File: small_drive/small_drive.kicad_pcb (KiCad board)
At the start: 2 copper layers, 100 x 80 mm, 159 parts, among them J1 DB9, J2 DB15, M1 SiR826DP, M2 SiR826DP, M3 SiR826DP, M4 SiR826DP, M5 SiR826DP, M6 SiR826DP, P1 CONN_01X04, P2 CONN_01X04, P3 CONN_01X04, P4 CONN_01X04, P5 CONN_01X02, P6 CONN_01X02, P7 CONN_01X02, P8 CONN_01X01, U1 XMC4400-F64x512, U10 LM5106, U11 ACS711KLCTR-12AB-T, U12 ACS711ELCTR-25AB-T, U13 ACS711KLCTR-12AB-T, U14 AD8226, U15 MAX3096, U16 AMC1203, U17 7805, U18 LT1764EQ, U19 KSZ8081, U2 ips511g, U20 ETH100_MAG, U3 ips511g, U4 LTC2850, U5 AD8226, U6 LT1764EQ, U7 MC33074DTBR2, U8 LM5106, U9 LM5106, X1 NKE1212DC, X2 NKE1212DC, X3 HCPL0201, X4 HCPL0201, X5 HCPL0201, X6 HCPL0201, Y1 12MHz, Y2 25MHz

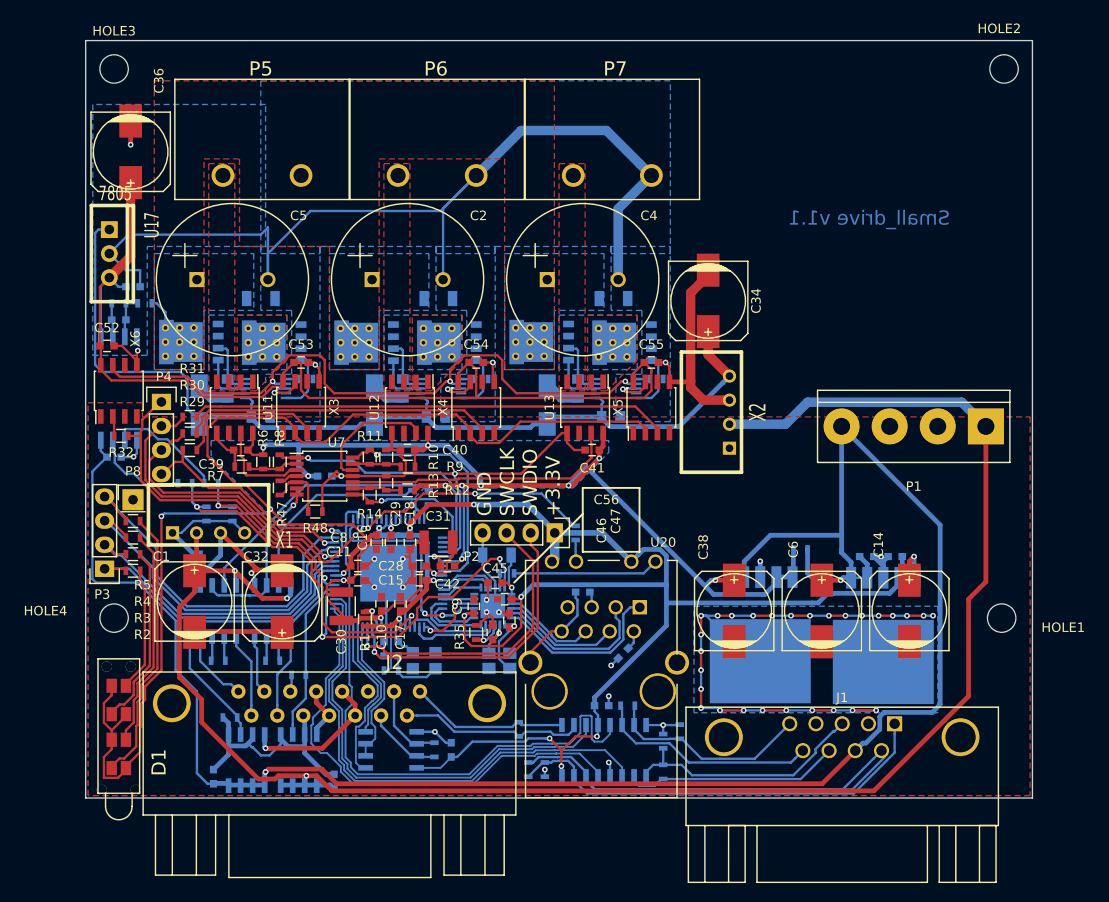
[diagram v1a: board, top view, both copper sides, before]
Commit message: Fully routed PCB with 100-pin package
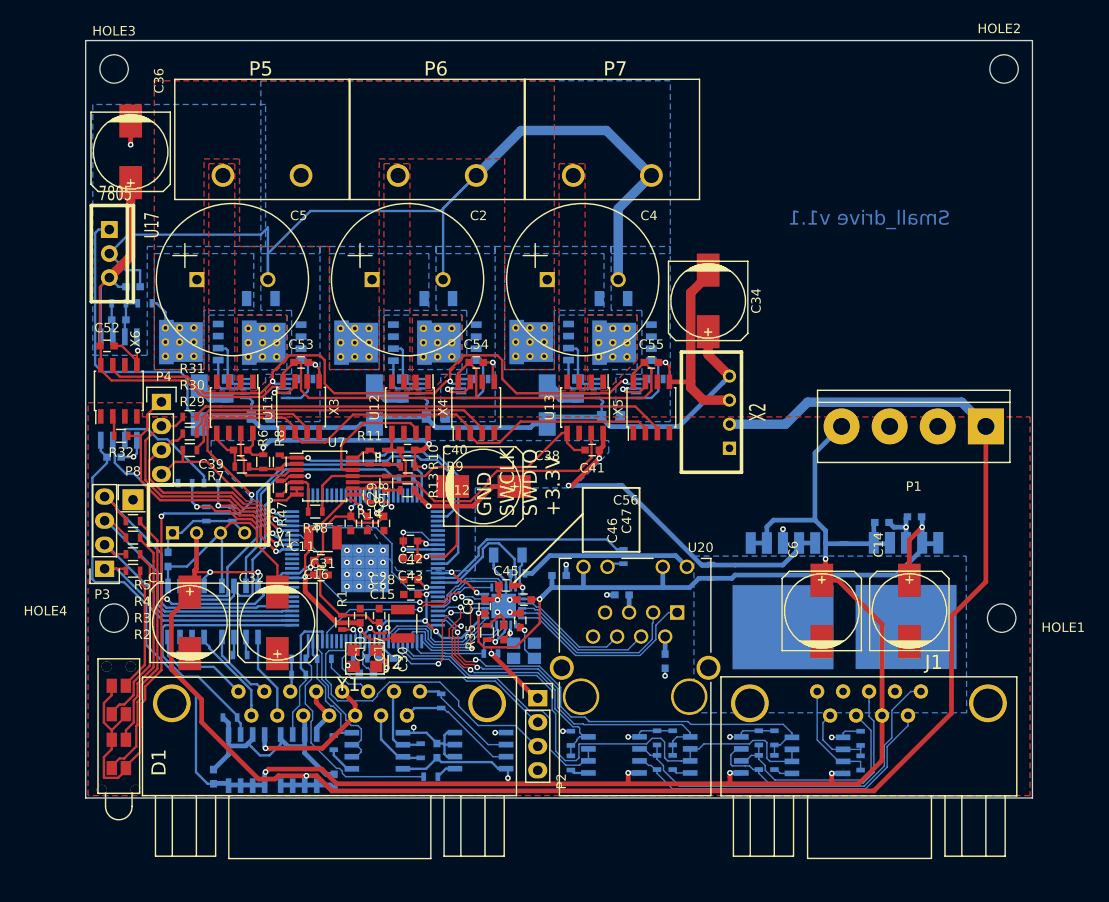
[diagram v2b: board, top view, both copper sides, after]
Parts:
- added R49: 1k, Resistors_SMD:R_0603, B.Cu at (81.8, 168.8)
- added R50: 510, Resistors_SMD:R_0603, B.Cu at (111.8, 180.2)
- added R51: 510, Resistors_SMD:R_0603, B.Cu at (101.0, 180.2)
- added R52: 510, Resistors_SMD:R_0603, B.Cu at (90.2, 180.3)
- added R53: 1k, Resistors_SMD:R_0603, B.Cu at (61.5, 169.3)
- added R54: 1k, Resistors_SMD:R_0603, B.Cu at (101.0, 177.7)
- added R55: 1k, Resistors_SMD:R_0603, B.Cu at (90.2, 177.7)
- added R56: 510, Resistors_SMD:R_0603, B.Cu at (75.5, 181.8)
- added R57: 510, Resistors_SMD:R_0603, B.Cu at (65.2, 178.2)
- added R58: 1k, Resistors_SMD:R_0603, B.Cu at (64.2, 169.3)
- added R59: 1k, Resistors_SMD:R_0603, B.Cu at (111.8, 177.7)
- added U21: MAX3463, Housings_SOIC:SOIC-8_3.9x4.9mm_Pitch1.27mm, B.Cu at (116.3, 179.5)
- added U22: MAX3463, Housings_SOIC:SOIC-8_3.9x4.9mm_Pitch1.27mm, B.Cu at (105.5, 179.4)
- added U23: MAX3463, Housings_SOIC:SOIC-8_3.9x4.9mm_Pitch1.27mm, B.Cu at (94.8, 179.4)
- C43, Y1: moved to F.Cu
- J1: footprint Connectors_Amphenol:DB9FC_HD-20 -> 00_Passives:DB9F_ebay
- J2: footprint Connectors_Amphenol:DB15F_HD20_SIZE2 -> 00_Passives:DB15F_ebay
- R22, R23: value R -> 4.7k
- R25, R26: value 1k -> 510
- R27, R28: value 510 -> 1k
- U1: value XMC4400-F64x512 -> XMC4400-F100; footprint Housings_QFP:LQFP-64-1EP_10x10mm_Pitch0.5mm -> Housings_QFP:TQFP-100-1EP_14x14mm_Pitch0.5mm
- U12: value ACS711ELCTR-25AB-T -> ACS711ELCTR-12AB-T
- U15: value MAX3096 -> MAX3463; footprint Housings_SOIC:SOIC-16_3.9x9.9mm_Pitch1.27mm -> Housings_SOIC:SOIC-8_3.9x4.9mm_Pitch1.27mm
- U4: value LTC2850 -> MAX3463
- moved R43 33.5 mm to (120.8, 177.7), turned to 270 degrees
- moved C38 29.6 mm to (81.0, 151.1), turned to 0 degrees
- moved R38 25.3 mm to (120.8, 180.3), turned to 90 degrees
- moved P2 17.6 mm to (86.8, 173.5), turned to 0 degrees
- moved C57 14.5 mm to (89.0, 160.5)
- moved R40 13.6 mm to (99.3, 180.2), turned to 270 degrees
- moved U15 13.0 mm to (80.7, 179.0), turned to 0 degrees
- moved C43 12.5 mm to (73.3, 158.7), turned to 180 degrees
- moved C31 12.2 mm to (64.0, 156.5), turned to 0 degrees
- moved R39 10.1 mm to (110.1, 180.2), turned to 270 degrees
- moved R46 9.73 mm to (105.0, 160.1), turned to 90 degrees
- moved R24 8.73 mm to (76.5, 173.8)
- moved R42 8.38 mm to (110.1, 177.7)
- moved C30 6.76 mm to (72.5, 165.6)
- moved Y1 6.25 mm to (68.5, 169.2), turned to 0 degrees
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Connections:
- C58 pad 1: +3.3V -> +5V
- R25 pad 1: /MDAT -> /MCLK
- R26 pad 1: /MCLK -> /MDAT
- R27 pad 1: /MCLK -> /MDAT
- R28 pad 1: /MDAT -> /MCLK
- R41 pad 2: /~B -> /~A
- R42 pad 2: /~Z -> /B
- R43 pad 2: /~A -> /Z
- U1 pad 1: /ETH_CRS_DVA -> Net-(U1-Pad1)
- U1 pad 11: Net-(U1-Pad11) -> +3.3V
- U1 pad 12: Net-(U1-Pad12) -> /VddC
- U1 pad 13: +3.3V -> Net-(U1-Pad13)
- U1 pad 14: /ENC_SIN -> Net-(U1-Pad14)
- U1 pad 15: /ENC_SIN -> Net-(U1-Pad15)
- U1 pad 16: /ENC_COS -> Net-(U1-Pad16)
- U1 pad 17: Net-(U1-Pad17) -> +3.3V
- U1 pad 2: /ENC_RXD2 -> Net-(U1-Pad2)
- U1 pad 20: /CUR0 -> Net-(U1-Pad20)
- U1 pad 21: GND -> Net-(U1-Pad21)
- U1 pad 22: +3.3VADC -> Net-(U1-Pad22)
- U1 pad 23: Net-(U1-Pad23) -> /ENC_SIN
- U1 pad 24: /CUR1 -> /ENC_SIN
- U1 pad 25: /VddC -> /ENC_COS
- U1 pad 26: +3.3V -> Net-(U1-Pad26)
- U1 pad 27: /ETH0_TXD1 -> /CUR0
- U1 pad 28: /ETH0_TXD0 -> Net-(U1-Pad28)
- U1 pad 29: /ETH0_TX_EN -> Net-(U1-Pad29)
- U1 pad 3: /HBEN -> Net-(U1-Pad3)
- U1 pad 30: /ETH0_RXERA -> Net-(U1-Pad30)
- U1 pad 31: /ETH0_RXD1A -> Net-(U1-Pad31)
- U1 pad 32: /ETH0_RXD0A -> GND
- U1 pad 33: /ETH0_CLK_RMIIA -> +3.3VADC
- U1 pad 34: /ETH0_MDIO -> GND
- U1 pad 35: /ETH0_MDC -> +3.3VADC
- U1 pad 36: /MDAT -> Net-(U1-Pad36)
- U1 pad 37: GND -> /CUR1
- U1 pad 38: +3.3V -> Net-(U1-Pad38)
- U1 pad 39: Net-(C49-Pad2) -> /ETH0_INT
- U1 pad 4: /LED4 -> Net-(U1-Pad4)
- U1 pad 40: Net-(R18-Pad2) -> /LED4
- U1 pad 41: GND -> /ETH0_~RST
- U1 pad 43: Net-(R1-Pad2) -> +3.3V
- U1 pad 44: /SWDIO -> Net-(U1-Pad44)
- U1 pad 45: /SWCLK -> /ETH0_TXD1
- U1 pad 46: /ENC_DIR -> /ETH0_TXD0
- U1 pad 47: /ENC_TXD -> /ENC1_A/DATA
- U1 pad 48: /ENC_RXD -> /ENC1_B/CLK
- U1 pad 49: /ENC_A -> /ENC1_Z/SELECT
- U1 pad 50: /ENC_B -> Net-(U1-Pad50)
- U1 pad 51: /ENC_Z -> /ETH0_CLK_RMII
- U1 pad 52: /ETH0_~RST -> /ETH0_MDIO
- U1 pad 53: /ENC_12V -> /ETH0_MDC
- U1 pad 54: /MCLK -> /ENC1_CDIR
- U1 pad 55: /VddC -> /ENC1_DDIR
- U1 pad 56: +3.3V -> /ETH0_CRS_DV
- U1 pad 57: /ENC_5V -> /ETH0_RXD1
- U1 pad 58: /LED0 -> /ETH0_RXD0
- U1 pad 59: /LED1 -> GND
- U1 pad 60: /HB2 -> +3.3V
- U1 pad 61: /HB0 -> Net-(C49-Pad2)
- U1 pad 62: /LED2 -> Net-(R18-Pad2)
- U1 pad 63: /HB1 -> GND
- U1 pad 64: /LED3 -> /VddC
- U1 pad 8: +3.3V -> Net-(U1-Pad8)
- U1 pad 9: /VddC -> Net-(U1-Pad9)
- U15 pad 1: /ENC_RXN -> Net-(R56-Pad2)
- U15 pad 2: /ENC_RXP -> GND
- U15 pad 3: /ENC_Z -> GND
- U15 pad 4: +3.3V -> GND
- U15 pad 5: /ENC_RXD2 -> GND
- U15 pad 6: /Z -> /ENC_RXN
- U15 pad 7: /~Z -> /ENC_RXP
- U15 pad 8: GND -> +5V
- U19 pad 12: /ETH0_RXD1A -> /ETH0_RXD1
- U19 pad 13: /ETH0_RXD0A -> /ETH0_RXD0
- U19 pad 15: /ETH_CRS_DVA -> /ETH0_CRS_DV
- U19 pad 16: /ETH0_CLK_RMIIA -> /ETH0_CLK_RMII
- U19 pad 17: /ETH0_RXERA -> /ETH0_RXER
- U19 pad 18: Net-(U19-Pad18) -> /ETH0_INT
- U4 pad 1: /ENC_RXD -> Net-(R57-Pad1)
- U4 pad 2: /ENC_DIR -> /ENC0_DIR
- U4 pad 3: /ENC_DIR -> /ENC0_DIR
- U4 pad 4: /ENC_TXD -> /ENC0_TXD
- U4 pad 8: +3.3V -> +5V
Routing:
- net GND: track 263.9 -> 194.2 mm, vias 47 -> 36
- net /ENC_RXD2: track 65.1 -> 0.00 mm
- net /ENC1_CDIR: track 0.00 -> 58.9 mm
- net +3.3V: track 326.7 -> 270.5 mm
- net /ENC_B: track 52.5 -> 0.00 mm
- net /ENC_A: track 50.7 -> 0.00 mm
- net /ENC1_Z/SELECT: track 0.00 -> 48.9 mm, vias 0 -> 2
- net /ENC_Z: track 48.5 -> 0.00 mm
- net /ENC1_B/CLK: track 0.00 -> 40.1 mm, vias 0 -> 2
- net /A: track 74.6 -> 34.9 mm
- net /ENC1_A/DATA: track 0.00 -> 31.1 mm, vias 0 -> 2
- net /ENC1_DDIR: track 0.00 -> 29.2 mm
- net /ENC0_RXD: track 0.00 -> 25.6 mm
- net /ETH0_RXER: track 0.00 -> 25.5 mm, vias 0 -> 2
- net /MDAT: track 37.0 -> 13.8 mm
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
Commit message: New small_drive, untested, unverified.
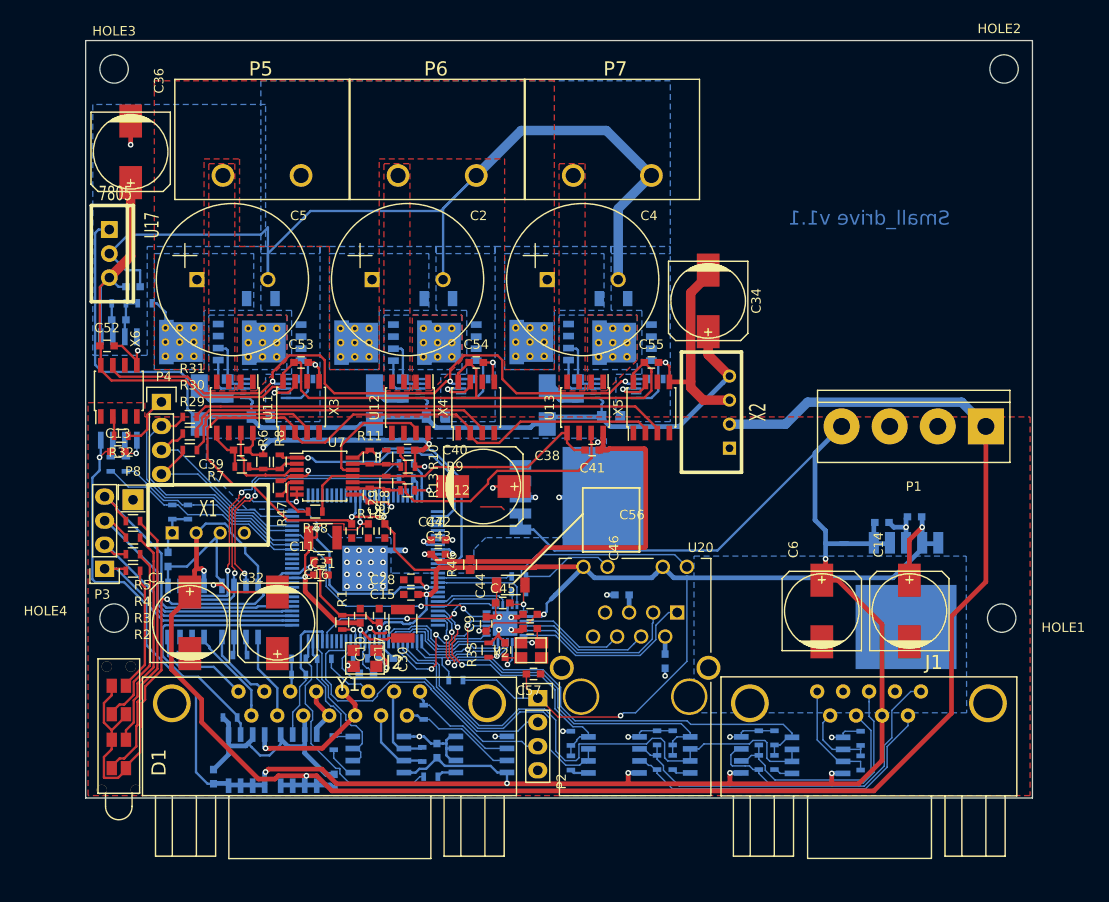
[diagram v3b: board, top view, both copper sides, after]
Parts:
- C13, C44, C57, R46, Y2: moved to F.Cu
- moved R46 25.5 mm to (79.6, 159.3)
- moved U18 24.7 mm to (90.0, 152.2), turned to 90 degrees
- moved R37 11.2 mm to (84.8, 160.6), turned to 0 degrees
- moved C57 10.7 mm to (86.3, 170.9)
- moved R26 9.22 mm to (43.2, 148.8), turned to 90 degrees
- moved R25 8.10 mm to (41.6, 148.8), turned to 90 degrees
- moved R27 4.70 mm to (49.8, 153.8)
- moved R49 4.64 mm to (78.1, 171.6)
- moved R28 3.61 mm to (48.1, 153.8)
- moved C44 3.18 mm to (83.9, 161.5)
- moved C43 2.98 mm to (76.2, 158.2), turned to 0 degrees
- moved C42 2.95 mm to (76.2, 156.8), turned to 0 degrees
- moved R24 2.21 mm to (74.7, 174.9)
- moved R36 1.98 mm to (84.8, 162.2)
- moved C45 1.88 mm to (83.0, 163.4)
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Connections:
- U1 pad 38: Net-(U1-Pad38) -> +3.3VADC
- U1 pad 39: /ETH0_INT -> Net-(U1-Pad39)
- U1 pad 97: /HB1 -> /HB0
- U1 pad 99: /HB0 -> /HB1
- U19 pad 18: /ETH0_INT -> Net-(U19-Pad18)
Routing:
- net +5V: track 199.5 -> 234.1 mm, vias 6 -> 7
- net +3.3V: track 270.5 -> 299.5 mm, vias 14 -> 10
- net /LED4: track 22.2 -> 7.86 mm
- net +3.3VADC: track 99.2 -> 85.2 mm
- net Net-(R26-Pad2): track 12.3 -> 1.84 mm
- net GND: track 194.2 -> 184.2 mm, vias 36 -> 37
- net Net-(R37-Pad2): track 1.82 -> 10.3 mm
- net Net-(R25-Pad2): track 10.2 -> 1.88 mm
- net /MDAT: track 13.8 -> 20.8 mm, vias 2 -> 0
- net /MCLK: track 16.3 -> 22.6 mm, vias 2 -> 0
- net /ETH0_INT: track 6.00 -> 0.00 mm, vias 2 -> 0
- net +12V: track 186.8 -> 191.0 mm, vias 3 -> 2
- net -12V: track 27.7 -> 23.5 mm, vias 0 -> 1
- net /HB1: track 23.9 -> 20.1 mm, vias 1 -> 0
- net /ETH0_~RST: track 14.1 -> 10.5 mm
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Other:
- board text removed: "GND SWCLK SWDIO +3.3V"

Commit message: Adding more advanced speed observer model.
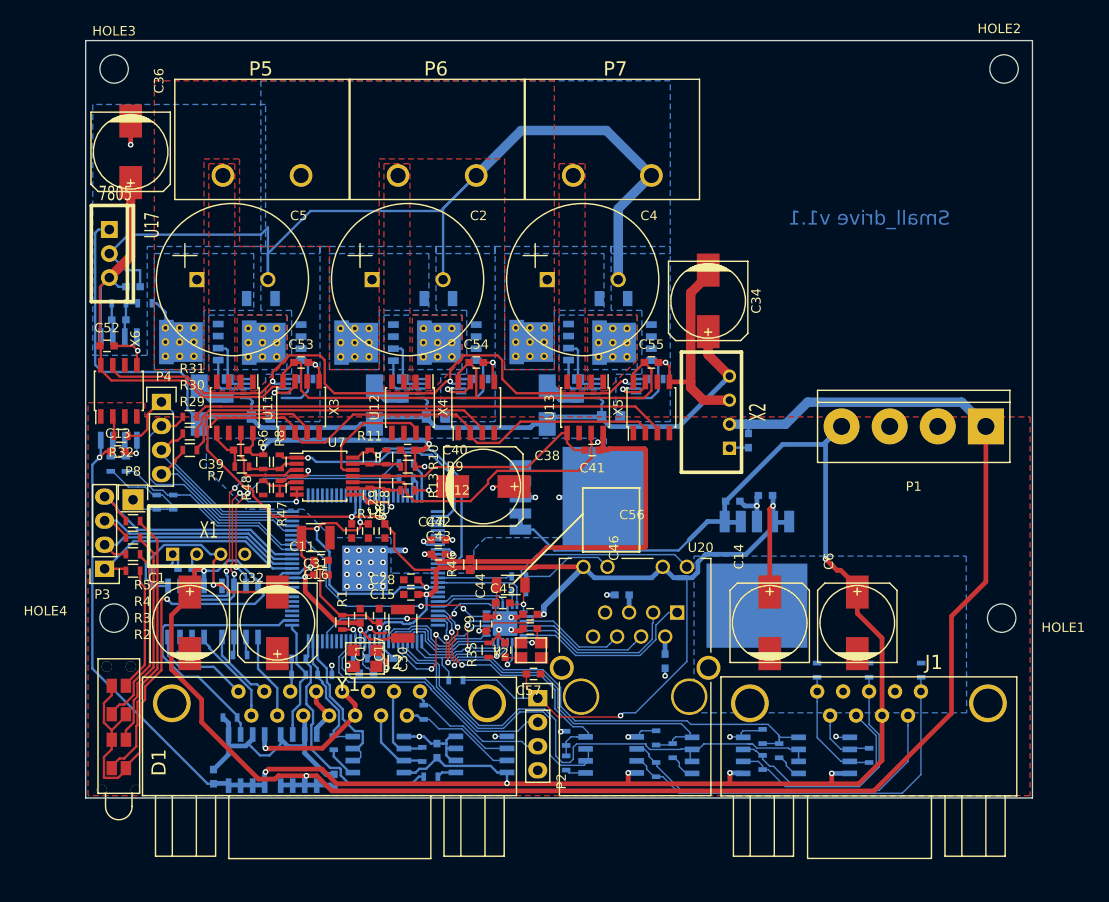
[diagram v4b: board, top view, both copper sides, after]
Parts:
- added C60: 100nF, Capacitors_SMD:C_0603, B.Cu at (109.0, 146.2)
- added C61: 100nF, Capacitors_SMD:C_0603, B.Cu at (49.5, 159.8)
- moved R41 28.8 mm to (127.2, 170.5)
- moved C12 15.9 mm to (107.3, 152.7)
- moved C59 15.9 mm to (110.8, 152.1)
- moved U6 15.9 mm to (109.9, 159.9)
- moved C14 14.8 mm to (111.2, 165.5)
- moved R42 13.7 mm to (121.8, 170.5)
- moved R43 8.54 mm to (116.2, 170.5)
- moved R48 6.04 mm to (57.8, 151.2), turned to 270 degrees
- moved C6 3.95 mm to (120.5, 165.5)
- moved C33 2.59 mm to (46.0, 160.8)
- moved X1 2.25 mm to (52.0, 158.2)
- moved R28 1.96 mm to (46.5, 152.8)
- moved R27 1.87 mm to (48.2, 152.8)
- moved R54 1.75 mm to (99.2, 177.7)
- moved R58 1.70 mm to (64.2, 171.0)
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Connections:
- J1 pad 4: Net-(J1-Pad4) -> GND
- R42 pad 2: /B -> /~B
- R43 pad 2: /Z -> /~Z
- U1 pad 100: Net-(U1-Pad100) -> /HBEN
- U1 pad 72: /ENC_12V -> Net-(U1-Pad72)
- U1 pad 76: /ENC_5V -> /ENC_12V
- U1 pad 77: /LED0 -> /ENC_5V
- U1 pad 78: /LED1 -> Net-(U1-Pad78)
- U1 pad 79: /LED2 -> Net-(U1-Pad79)
- U1 pad 80: /LED3 -> Net-(U1-Pad80)
- U1 pad 88: Net-(U1-Pad88) -> /LED0
- U1 pad 89: Net-(U1-Pad89) -> /LED1
- U1 pad 90: Net-(U1-Pad90) -> /LED2
- U1 pad 91: Net-(U1-Pad91) -> /LED3
- U1 pad 94: /HBEN -> Net-(U1-Pad94)
- U22 pad 6: /~B -> /B
- U22 pad 7: /B -> /~B
- U23 pad 6: /~A -> /A
- U23 pad 7: /A -> /~A
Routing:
- net +5V: track 234.1 -> 222.4 mm
- net GND: track 184.2 -> 173.1 mm, vias 37 -> 38
- net +3.3V: track 299.5 -> 293.1 mm
- net /SWCLK: track 33.6 -> 27.9 mm
- net /LED3: track 31.5 -> 26.0 mm
- net /HBEN: track 32.8 -> 27.7 mm
- net /LED2: track 29.0 -> 24.7 mm
- net +12V: track 191.0 -> 187.5 mm
- net -12V: track 23.5 -> 26.4 mm
- net (no net): track 2.62 -> 0.00 mm
- net /~A: track 40.1 -> 42.6 mm
- net /LED1: track 26.6 -> 24.2 mm
- net /ENC1_CDIR: track 60.0 -> 57.9 mm
- net /ENC_12V: track 14.7 -> 12.7 mm
- net Net-(R47-Pad2): track 7.39 -> 5.55 mm
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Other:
- net class Default: trace_width 0.25 -> 0.15
